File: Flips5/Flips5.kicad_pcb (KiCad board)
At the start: 2 copper layers, 100 x 100 mm, 23 parts, among them IC1 FP2800A, IC2 FP2800A, IC3 FP2800A

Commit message: Switching back to V0.9
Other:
- board text added: "SRT Flips 5 V0.9 2018-11-16 github.com/cawapy/FlipSuite"
- board text removed: "SRT Flips 5 V1.0 2018-11-16 github.com/cawapy/FlipSuite"
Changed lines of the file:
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@@
     (title "Flips 5")
     (date 2018-11-16)
-    (rev V1.0)
+    (rev V0.9)
     (company SRT)
     (comment 1 "FlipDot Matrix Driver for Brose Interfaces (60P, 34P)")
@@
   (gr_line (start 88.9 62.865) (end 88.9 60.96) (angle 90) (layer F.SilkS) (width 0.2))
   (gr_line (start 81.28 62.865) (end 81.28 62.23) (angle 90) (layer F.SilkS) (width 0.2))
-  (gr_text "SRT Flips 5 V1.0 2018-11-16\ngithub.com/cawapy/FlipSuite" (at 64.135 78.105) (layer F.SilkS)
+  (gr_text "SRT Flips 5 V0.9 2018-11-16\ngithub.com/cawapy/FlipSuite" (at 64.135 78.105) (layer F.SilkS)
     (effects (font (size 1.5 1.5) (thickness 0.3)) (justify left))
   )

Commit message: Adding Rows 21-28 (extra connector; preliminary pin assignment)
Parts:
- added BRDA3: Conn_02x10_Odd_Even, Own:Pin_Header_Straight_Shrouded_2x10_Pitch2.54mm_ConvNumbering, F.Cu at (115.6, 78.7)
- moved REF*** 30.5 mm to (115.6, 109.2), turned to 90 degrees
- moved REF** 25.5 mm to (115.2, 95.2), turned to 90 degrees
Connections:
- IC2 pad 10: Net-(IC2-Pad10) -> /SY21
- IC2 pad 2: Net-(IC2-Pad2) -> /SY25
- IC2 pad 26: Net-(IC2-Pad26) -> /~RY22
- IC2 pad 27: Net-(IC2-Pad27) -> /~RY23
- IC2 pad 28: Net-(IC2-Pad28) -> /~RY24
- IC2 pad 29: Net-(IC2-Pad29) -> /~RY25
- IC2 pad 3: Net-(IC2-Pad3) -> /SY27
- IC2 pad 30: Net-(IC2-Pad30) -> /~RY27
- IC2 pad 31: Net-(IC2-Pad31) -> /~RY26
- IC2 pad 32: Net-(IC2-Pad32) -> /~RY28
- IC2 pad 33: Net-(IC2-Pad33) -> /~RY21
- IC2 pad 4: Net-(IC2-Pad4) -> /SY24
- IC2 pad 5: Net-(IC2-Pad5) -> /SY23
- IC2 pad 6: Net-(IC2-Pad6) -> /SY22
- IC2 pad 8: Net-(IC2-Pad8) -> /SY26
- IC2 pad 9: Net-(IC2-Pad9) -> /SY28
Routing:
- net /SY28: track 0.00 -> 64.8 mm, vias 0 -> 2
- net /~RY25: track 0.00 -> 64.0 mm, vias 0 -> 2
- net /SY26: track 0.00 -> 60.2 mm, vias 0 -> 2
- net /~RY22: track 0.00 -> 59.8 mm, vias 0 -> 3
- net /~RY23: track 0.00 -> 57.2 mm, vias 0 -> 2
- net /~RY24: track 0.00 -> 57.2 mm, vias 0 -> 3
- net /~RY27: track 0.00 -> 54.0 mm, vias 0 -> 2
- net /~RY26: track 0.00 -> 52.3 mm, vias 0 -> 3
- net /SY21: track 0.00 -> 52.2 mm, vias 0 -> 1
- net /~RY28: track 0.00 -> 49.3 mm, vias 0 -> 1
- net /SY23: track 0.00 -> 48.5 mm, vias 0 -> 1
- net /SY24: track 0.00 -> 45.9 mm, vias 0 -> 1
- net /SY22: track 0.00 -> 45.1 mm, vias 0 -> 1
- net /SY27: track 0.00 -> 43.2 mm, vias 0 -> 1
- net /~RY21: track 0.00 -> 42.1 mm, vias 0 -> 2
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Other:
- board text added: "FlipDot Matrix Driver for Brose Interfaces (60P+20P, 34P)"
- board text added: "Rows 15-20, 21-28 (shared)"
- board text removed: "FlipDot Matrix Driver for Brose Interfaces (60P, 34P)"
- board text removed: "Rows 15-20 (shared)"

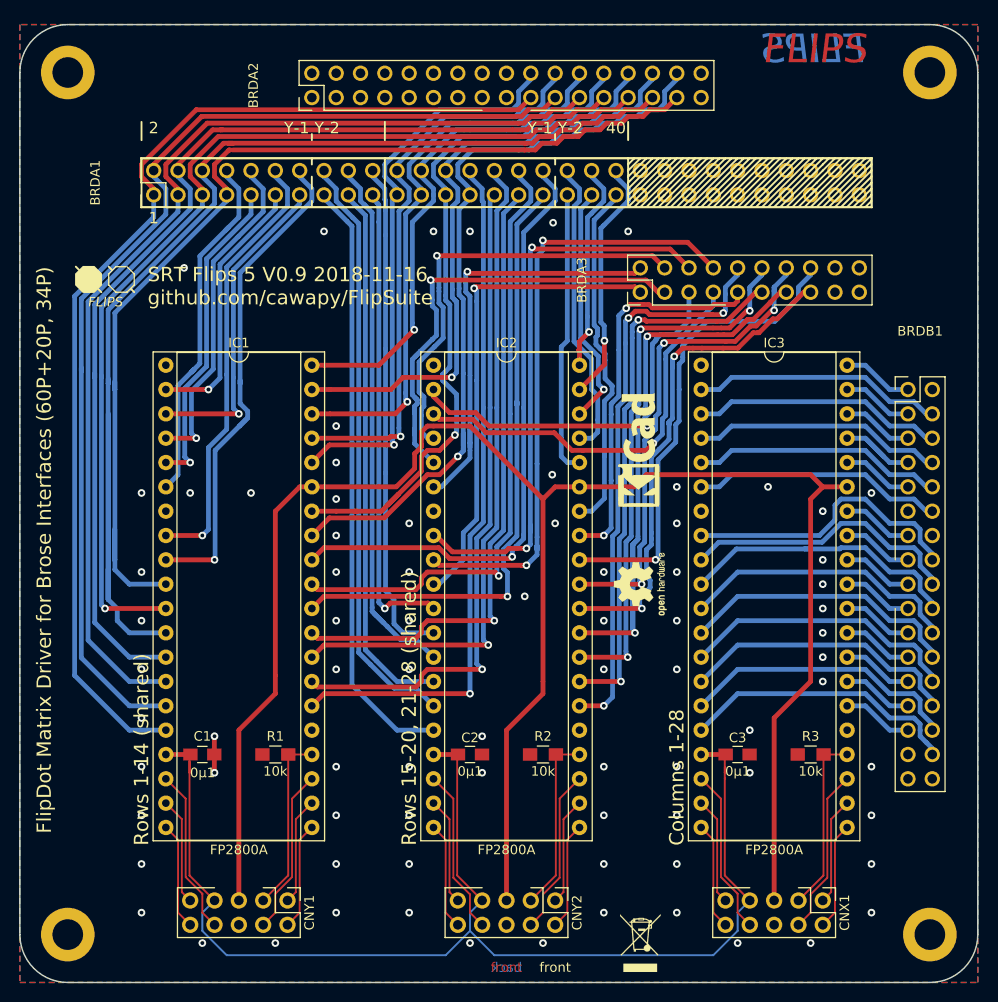
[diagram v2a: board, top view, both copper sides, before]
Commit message: adding "+20P" in silk screen and descriptions; adding 3d model for row driver; cleaning up traces
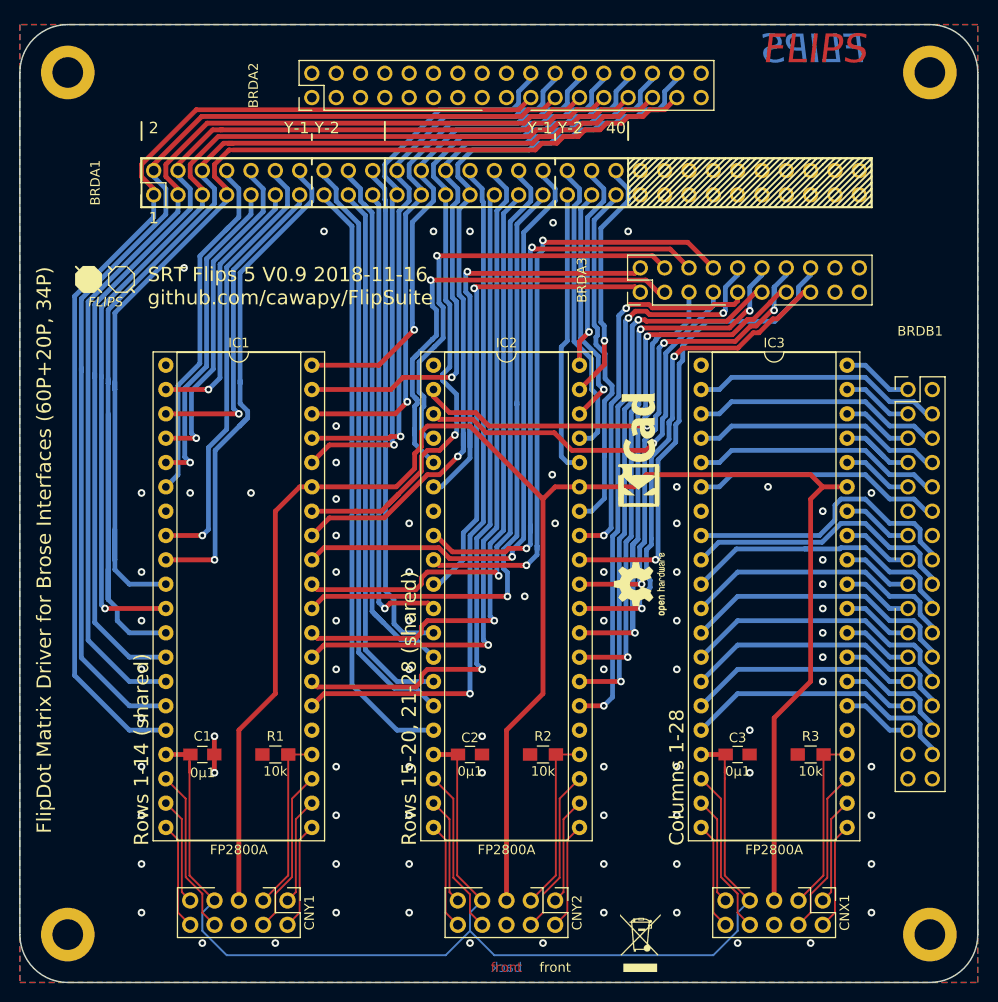
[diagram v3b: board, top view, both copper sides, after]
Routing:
- net /~RY27: track 54.0 -> 52.0 mm
- net /SY8: track 38.0 -> 37.2 mm
- net /SY23: track 48.5 -> 47.8 mm
- net /~RY5: track 76.8 -> 76.3 mm

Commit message: sorting traces
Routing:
- net /GND: track 3.91 -> 39.5 mm, vias 80 -> 93
- net /SY25: track 41.2 -> 32.3 mm, vias 1 -> 0
- net /~RY21: track 42.1 -> 37.8 mm, vias 2 -> 1
- net /SY27: track 43.2 -> 39.6 mm, vias 1 -> 0
- net /~RY28: track 49.3 -> 51.7 mm
- net /SY22: track 45.1 -> 47.2 mm
- net /~RY27: track 52.0 -> 53.9 mm, vias 2 -> 1
- net /SY23: track 47.8 -> 49.6 mm
- net /SY14: track 52.6 -> 50.8 mm
- net /SY24: track 45.9 -> 47.6 mm
- net /~RY6: track 65.3 -> 63.7 mm
- net /SY21: track 52.2 -> 53.7 mm
- net /~RY23: track 57.2 -> 55.8 mm, vias 2 -> 1
- net /~RY7: track 79.5 -> 81.0 mm
- net /SY19: track 49.3 -> 50.6 mm
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
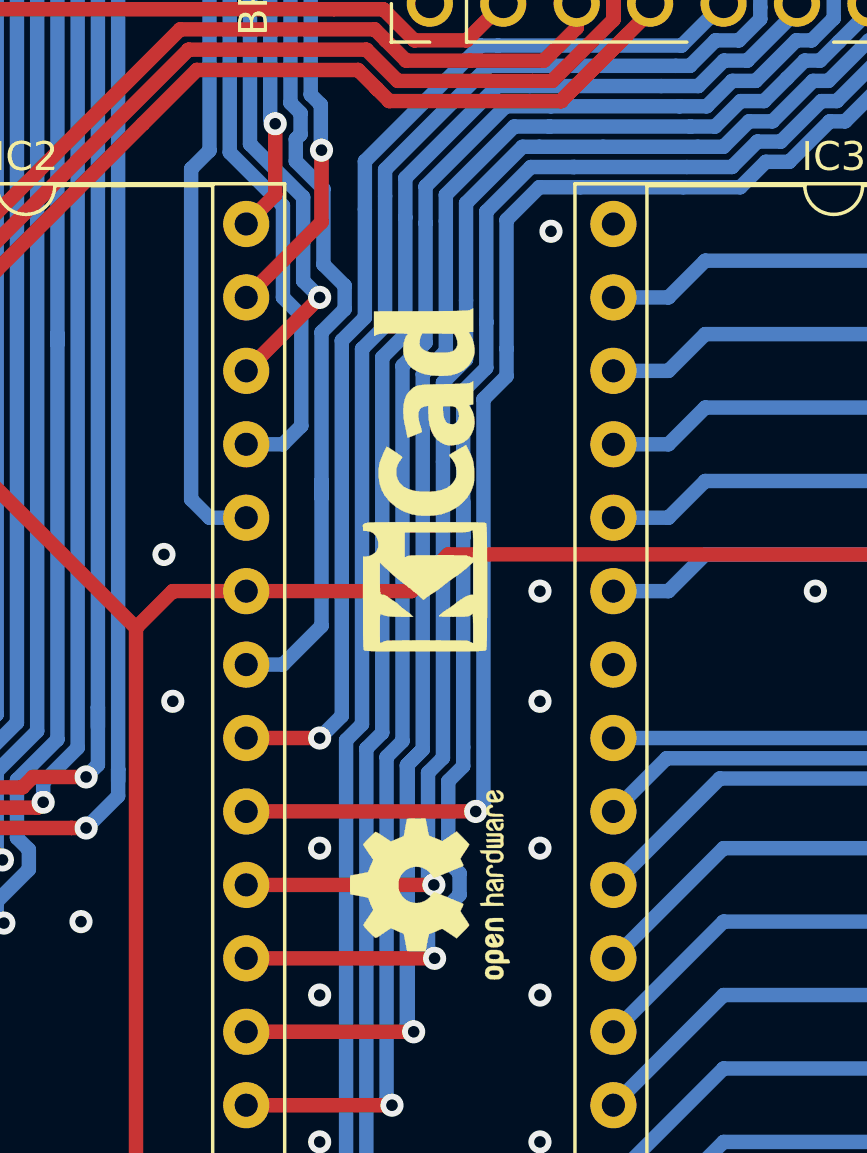
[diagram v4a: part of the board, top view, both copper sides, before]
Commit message: Fix icon footprint positions
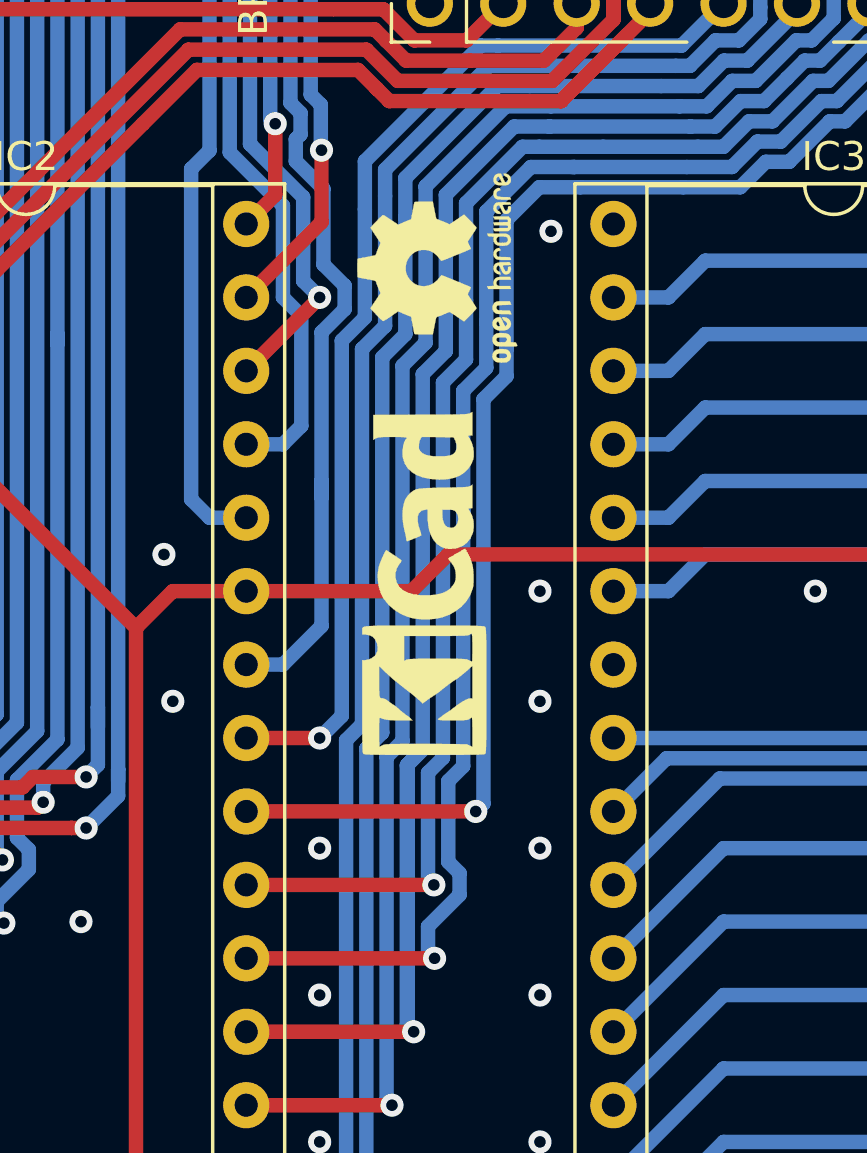
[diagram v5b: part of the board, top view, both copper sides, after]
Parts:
- moved REF*** 21.3 mm to (115.8, 87.9)
- moved REF** 3.58 mm to (115.2, 98.8)
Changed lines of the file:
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@@
   (layers
     (0 F.Cu signal)
-    (31 B.Cu signal)
+    (31 B.Cu signal hide)
     (32 B.Adhes user)
     (33 F.Adhes user)
@@
     (35 F.Paste user)
     (36 B.SilkS user)
-    (37 F.SilkS user hide)
+    (37 F.SilkS user)
     (38 B.Mask user)
     (39 F.Mask user)
@@
   )
   (module Symbols:Symbol_KiCAD-Logo_CopperAndSilkScreenTop (layer F.Cu)
-    (at 115.2144 95.2246 90)
+    (at 115.189 98.806 90)
     (descr "Symbol, KiCAD-Logo, Silk & Copper Top,")
     (tags "Symbol, KiCAD-Logo, Silk & Copper Top,")
@@
   )
   (module Symbols:OSHW-Logo2_7.3x6mm_SilkScreen (layer F.Cu)
-    (at 115.57 109.22 90)
+    (at 115.824 87.884 90)
     (descr "Open Source Hardware Symbol")
     (tags "Logo Symbol OSHW")

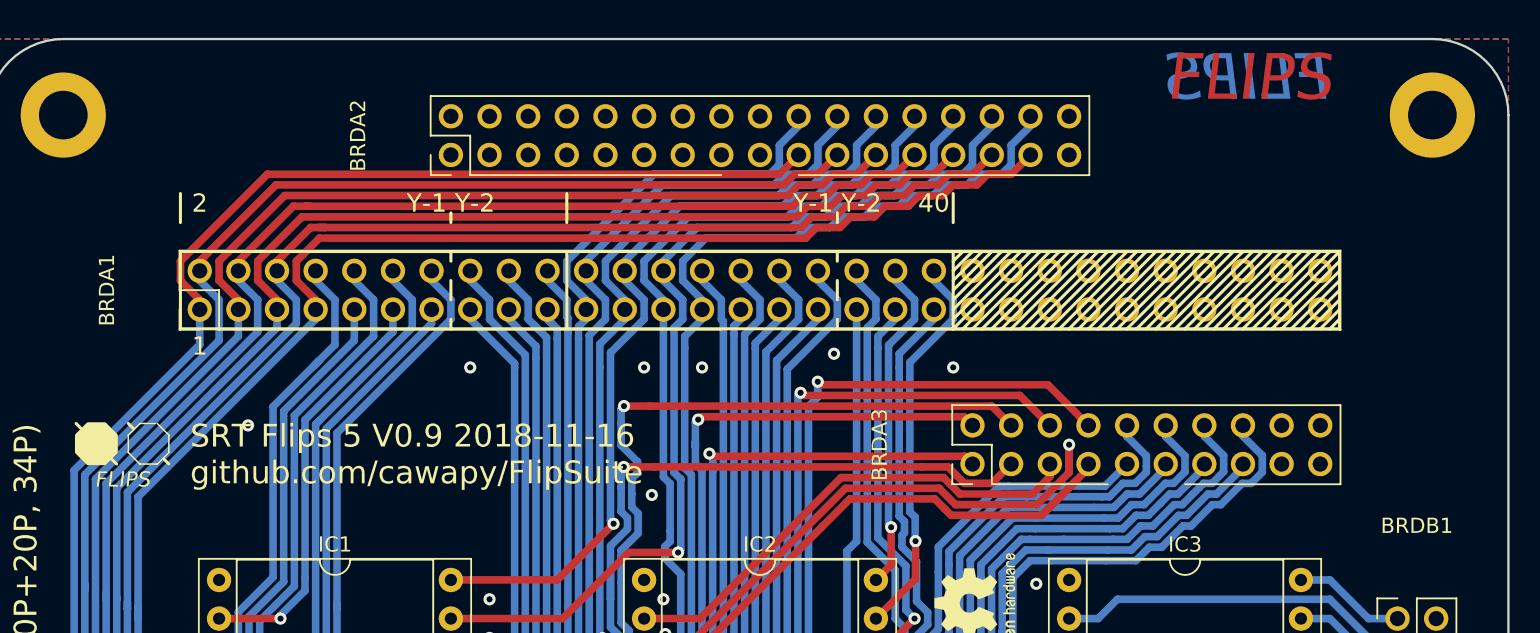
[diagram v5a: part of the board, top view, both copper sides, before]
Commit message: renaming connectors
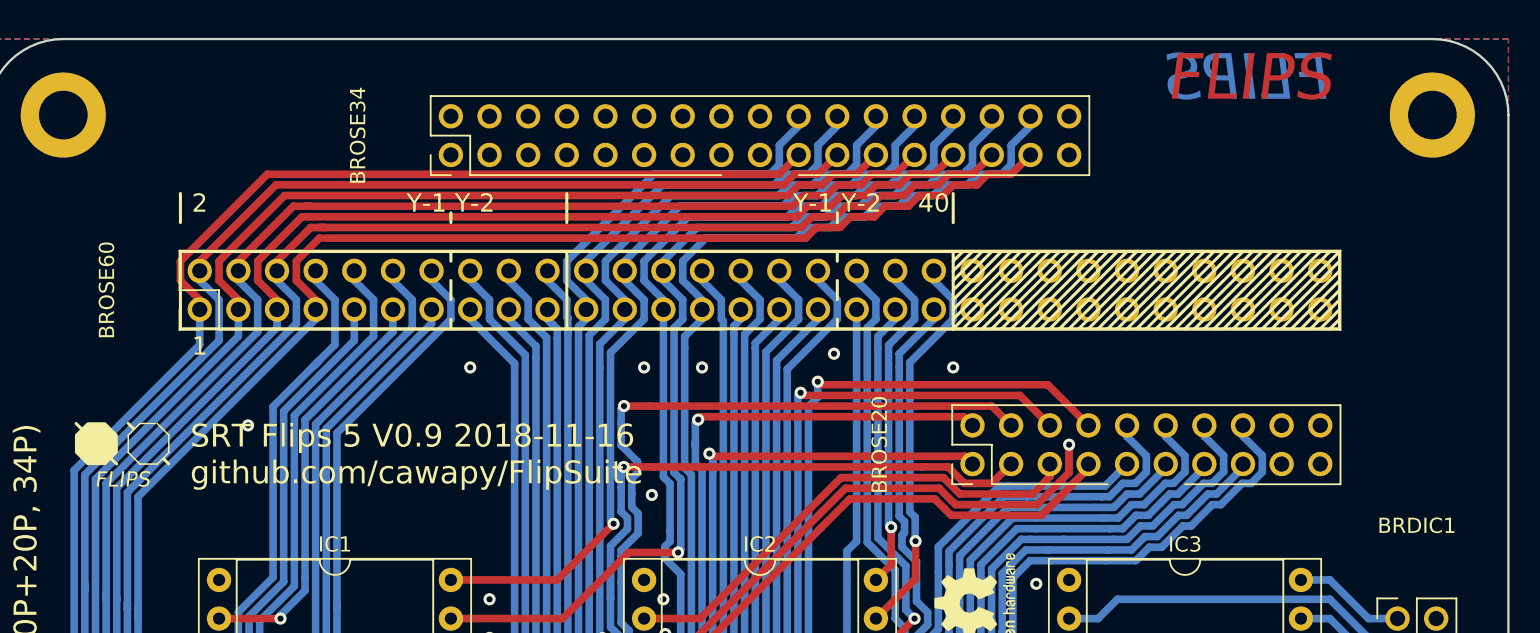
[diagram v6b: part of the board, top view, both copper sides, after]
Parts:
- renumbered BRDB1 to BRDIC1, BRDA3 to BROSE20, BRDA2 to BROSE34, BRDA1 to BROSE60

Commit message: change traces
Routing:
- net /SY8: track 37.2 -> 42.7 mm, vias 0 -> 1
- net /SY9: track 33.4 -> 36.7 mm
- net /SY10: track 34.8 -> 36.8 mm
- net /SY12: track 46.7 -> 48.6 mm
- net /SY14: track 50.8 -> 52.3 mm
- net /SY11: track 27.4 -> 28.3 mm
